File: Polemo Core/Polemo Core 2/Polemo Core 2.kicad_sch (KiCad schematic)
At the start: 174 parts, among them P1 Header-Male-2.54_2x2, P2 Header-Male-2.54_2x2, Q1 BC847_C2910145, Q2 MMBT5551LT1G, Q3 AO3401A, Q4 AO3401A, Q5 MMBT5551LT1G, U1 ATSAML21G18B-AUT, U10 74LVC1G08GV,125, U11 LT3014BHVES5#TRMPBF, U12 TXU0202DCUR, U13 TLV7031DBVR, U14 TLR341G-GTR, U15 803-87-006-10-001101, U2 XC6209F332MR-G, U3 MC14043BDR2G, U4 LMV793MFX/NOPB, U5 TPS7A2030PDBVR, U6 TLV3201AIDBVT, U7 OPA357AIDBVR, U8 TLR341G-GTR, U9 MF-ASML020/6-2, X1 32.768kHz

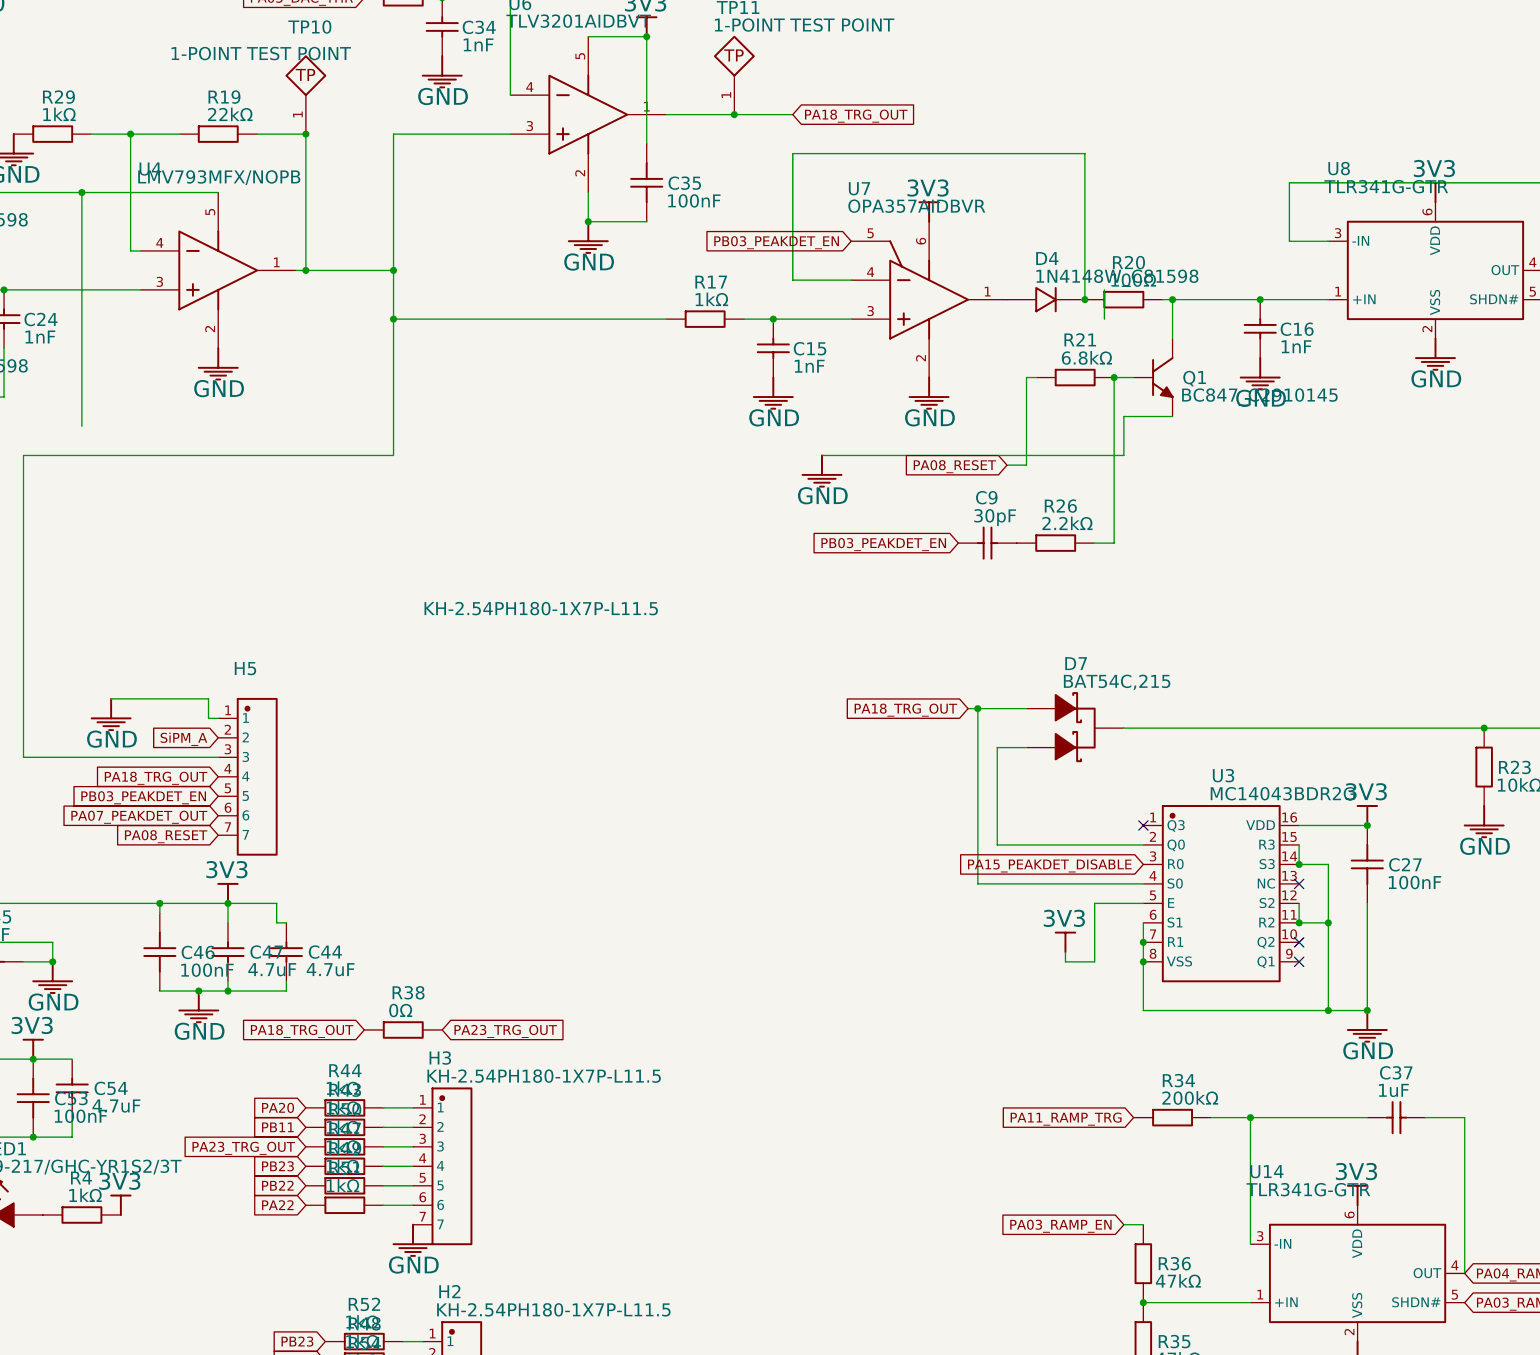
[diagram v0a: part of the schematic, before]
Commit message: Moved some components
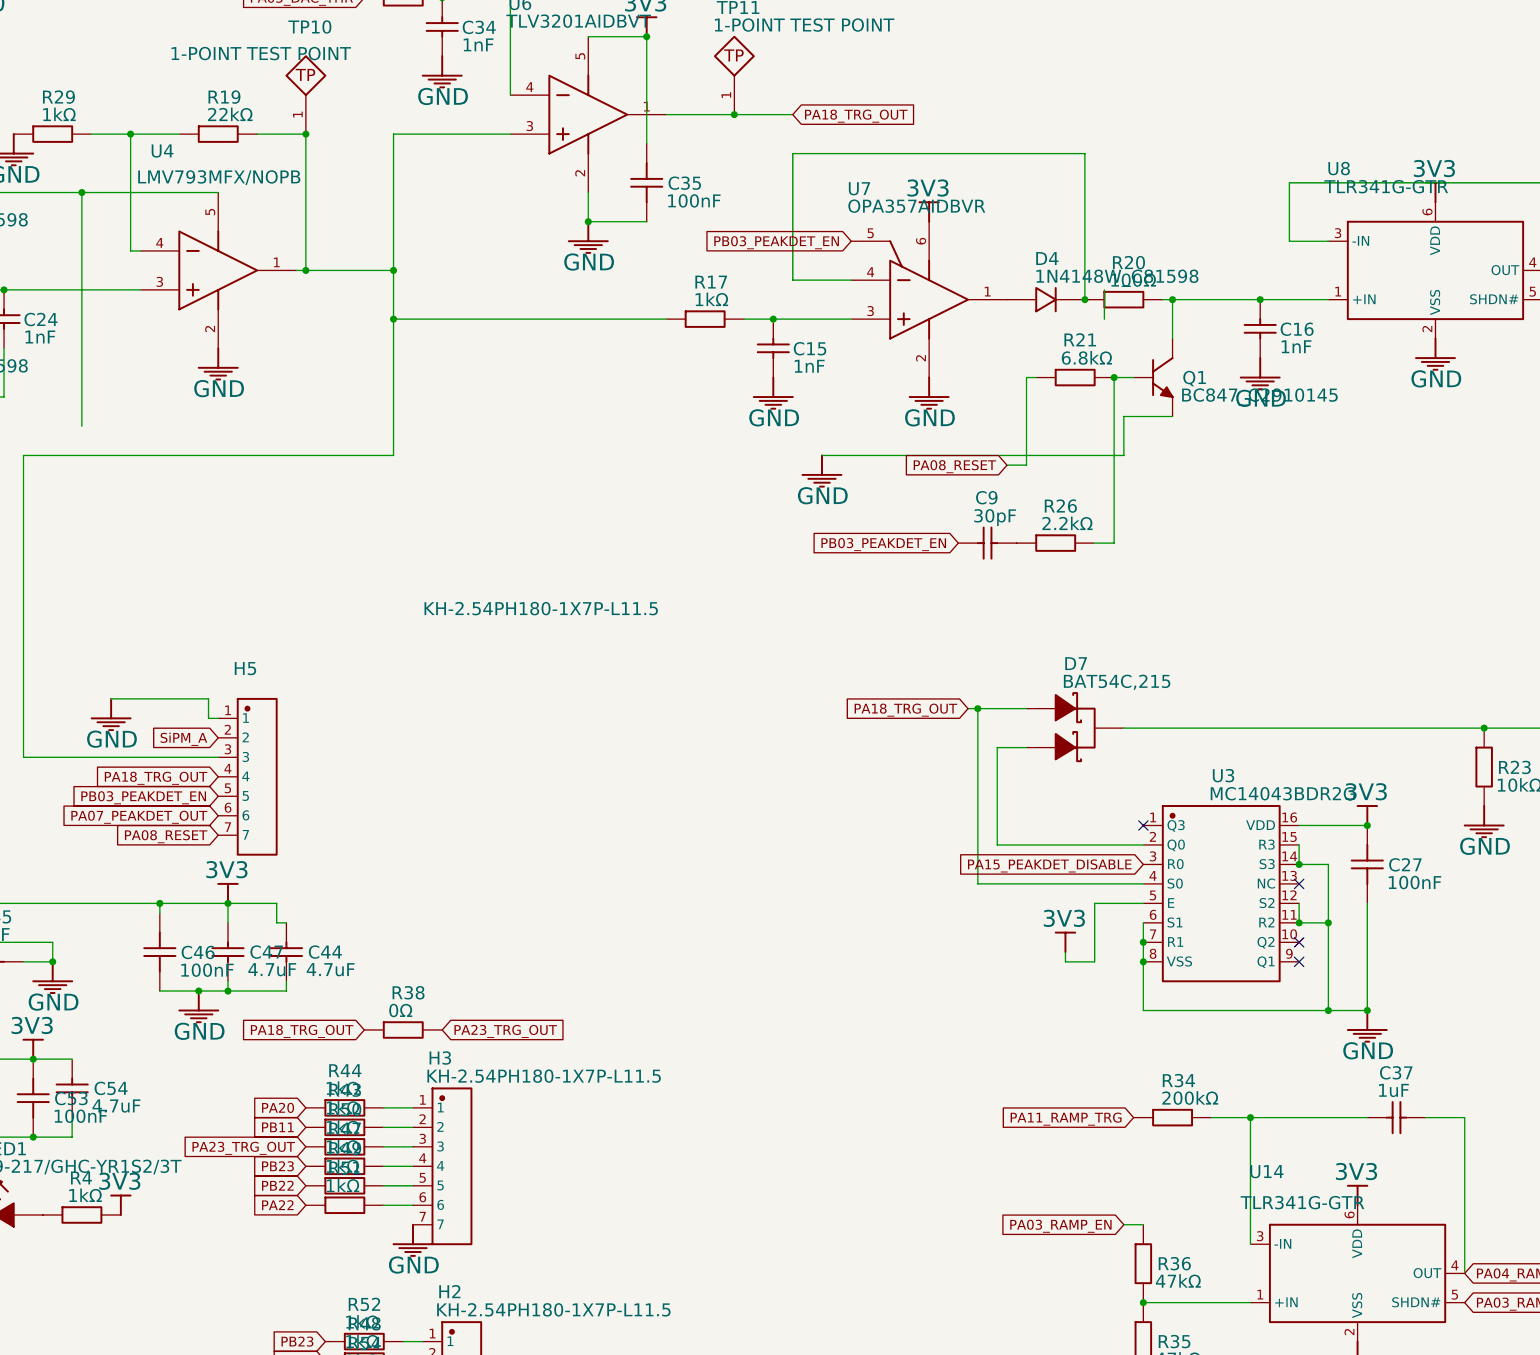
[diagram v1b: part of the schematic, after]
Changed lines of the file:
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@@
 		)
 		(property "Value" "TLR341G-GTR"
-			(at 501.142 176.1109 0)
+			(at 500.38 177.8 0)
 			(effects
 				(font
@@
 		(dnp no)
 		(property "Reference" "U4"
-			(at 356.5652 42.9895 0)
+			(at 358.14 40.64 0)
 			(effects
 				(font
